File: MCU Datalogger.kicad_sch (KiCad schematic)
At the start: 25 parts, among them U1 24LC1025, U2 24LC1025, U3 DS1337S_, U4 ATMEGA328P-AU, Y1 32.768 KHz, Y2 16 MHz

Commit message: Version for manufacturing
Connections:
- net Vcc: now also BT1.1 (+), C5.1, D2.2 (A), U4.18 (AVCC), U4.4 (VCC)
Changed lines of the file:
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@@
+	)
+	(label "Vcc"
+		(at 254 40.64 0)
+		(effects
+			(font
+				(size 1.27 1.27)
+			)
+			(justify left bottom)
+		)
 	)
 	(label "Vcc"

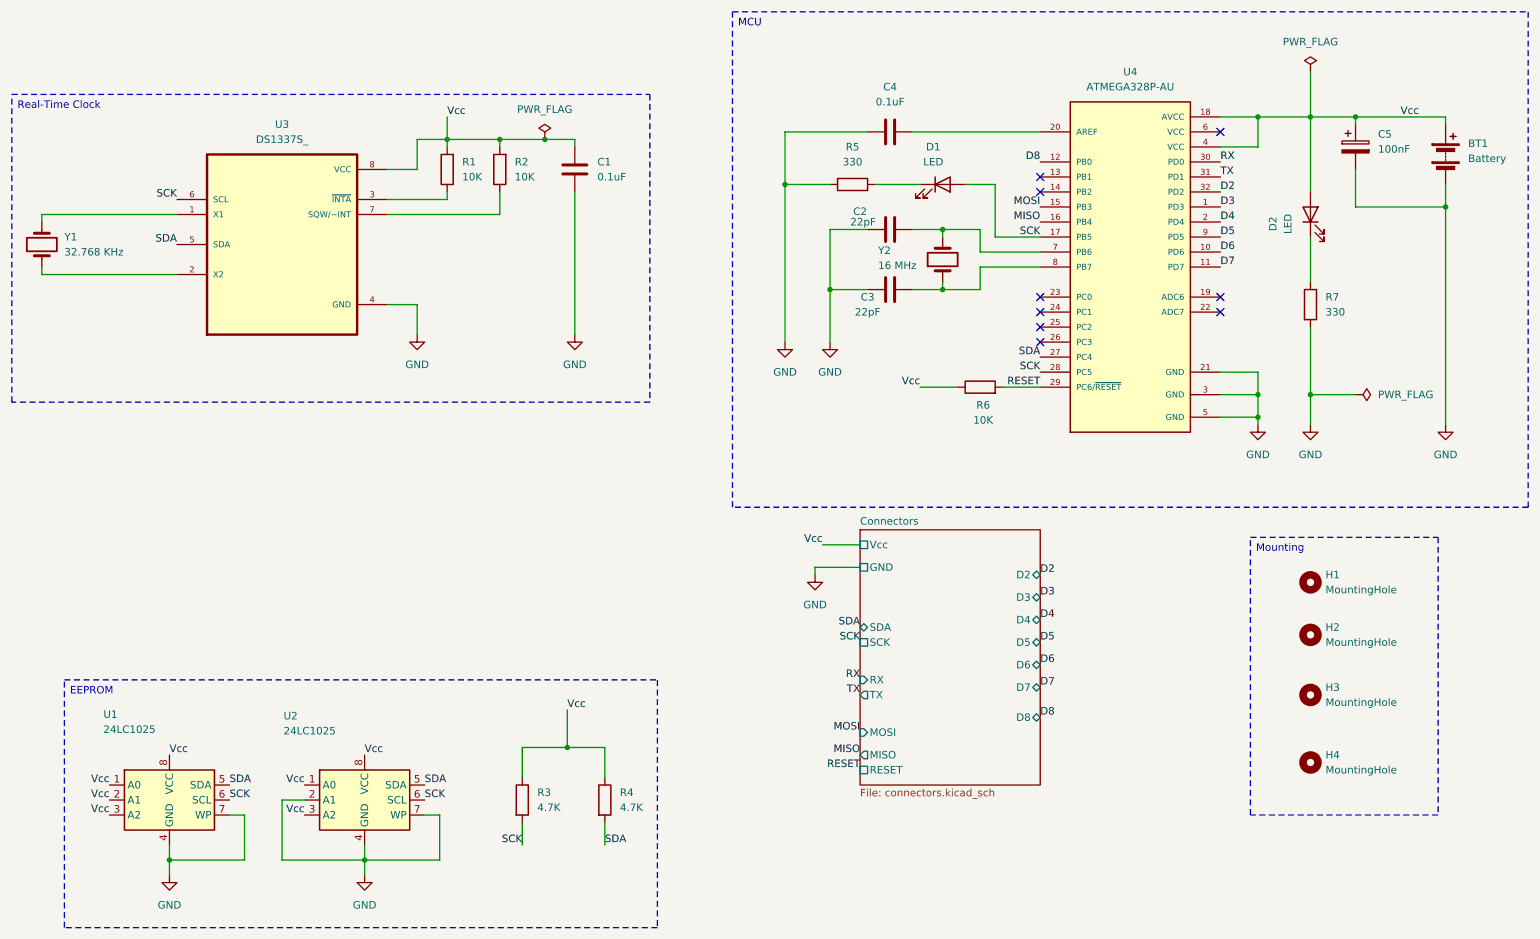
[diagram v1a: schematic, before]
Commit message: Fixed Bugs at 4layer
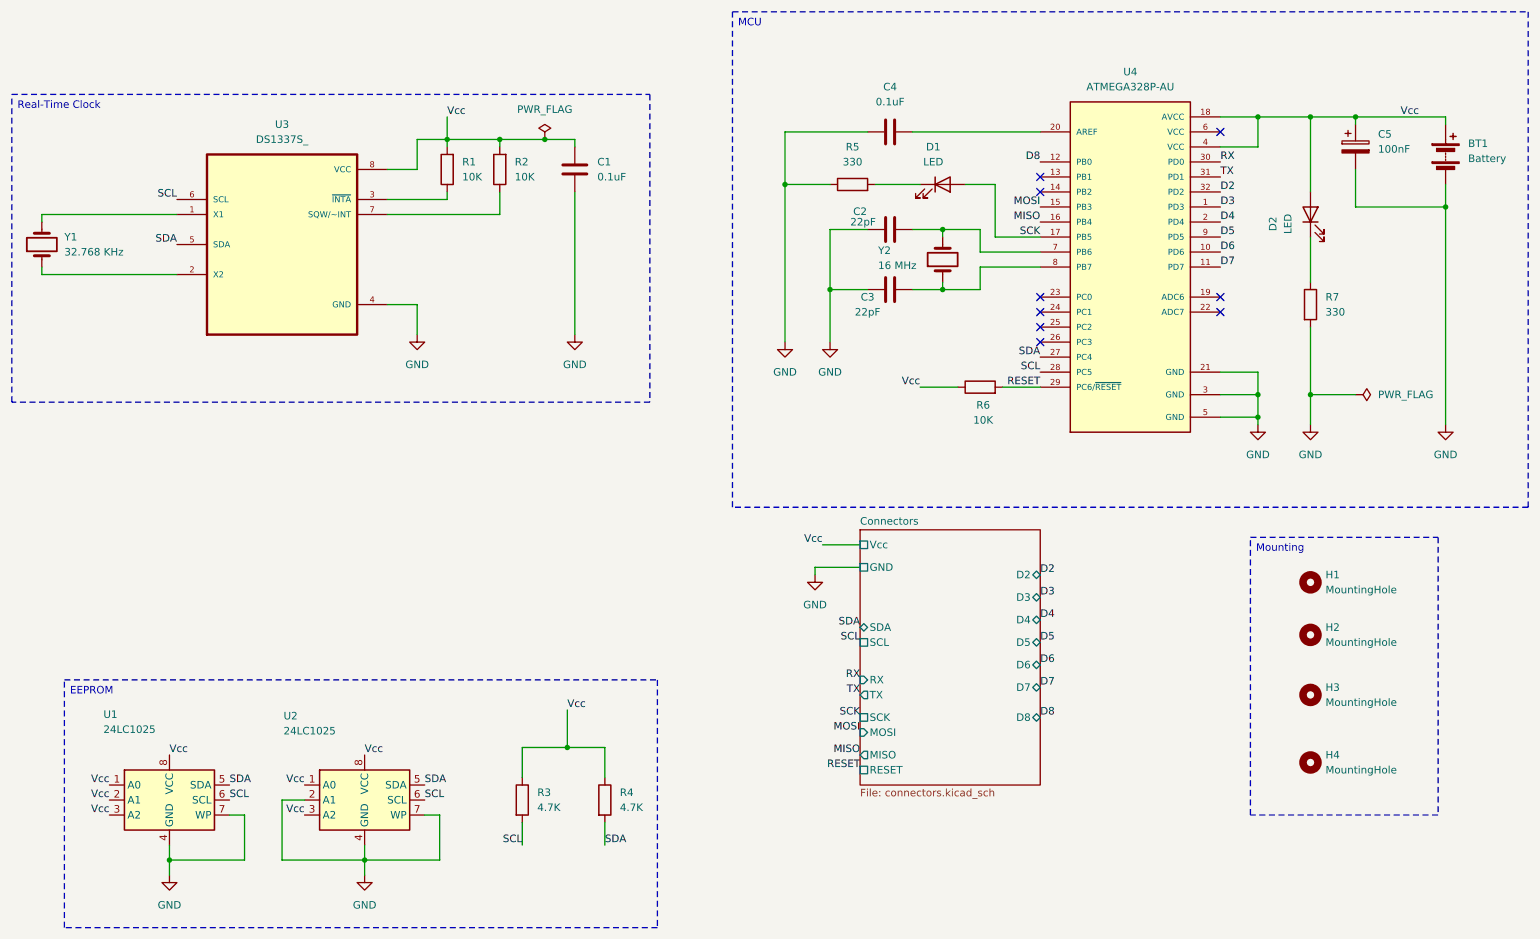
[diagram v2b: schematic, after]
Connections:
- net SCK: no longer R3.2, U1.6 (SCL), U2.6 (SCL), U3.6 (SCL), U4.28 (PC5)
- new net SCL: R3.2, U1.6 (SCL), U2.6 (SCL), U3.6 (SCL), U4.28 (PC5)
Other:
- sheet Connectors ports: added SCL; removed none
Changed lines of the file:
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@@
 	(wire
 		(pts
-			(xy 238.76 33.02) (xy 238.76 40.64)
-		)
-		(stroke
-			(width 0)
-			(type default)
-		)
-	)
-	(wire
-		(pts
 			(xy 82.55 57.15) (xy 101.6 57.15)
 		)
@@
 		)
 	)
+	(label "SCK"
+		(at 162.56 142.24 180)
+		(effects
+			(font
+				(size 1.27 1.27)
+			)
+			(justify right bottom)
+		)
+	)
 	(label "Vcc"
 		(at 35.56 153.67 180)
@@
 		)
 	)
-	(label "SCK"
+	(label "SCL"
 		(at 46.99 54.61 180)
 		(effects
@@
 		)
 	)
-	(label "SCK"
+	(label "SCL"
 		(at 55.88 156.21 0)
 		(effects
@@
 		)
 	)
-	(label "SCK"
+	(label "SCL"
 		(at 88.9 156.21 0)
 		(effects
@@
 		)
 	)
-	(label "SCK"
+	(label "SCL"
 		(at 193.04 83.82 180)
 		(effects
@@
 		)
 	)
-	(label "SCK"
+	(label "SCL"
 		(at 162.56 129.54 180)
 		(effects
@@
 		)
 	)
-	(label "SCK"
+	(label "SCL"
 		(at 105.41 163.83 180)
 		(effects
@@
 	)
 	(symbol
-		(lib_id "power:PWR_FLAG")
-		(at 238.76 33.02 0)
-		(unit 1)
-		(exclude_from_sim no)
-		(in_bom yes)
-		(on_board yes)
-		(dnp no)
-		(fields_autoplaced yes)
-		(property "Reference" "#FLG01"
-			(at 238.76 31.115 0)
-			(effects
-				(font
-					(size 1.27 1.27)
-				)
-				(hide yes)
-			)
-		)
-		(property "Value" "PWR_FLAG"
-			(at 238.76 27.94 0)
-			(effects
-				(font
-					(size 1.27 1.27)
-				)
-			)
-		)
-		(property "Footprint" ""
-			(at 238.76 33.02 0)
-			(effects
-				(font
-					(size 1.27 1.27)
-				)
-				(hide yes)
-			)
-		)
-		(property "Datasheet" "~"
-			(at 238.76 33.02 0)
-			(effects
-				(font
-					(size 1.27 1.27)
-				)
-				(hide yes)
-			)
-		)
-		(property "Description" "Special symbol for telling ERC where power comes from"
-			(at 238.76 33.02 0)
-			(effects
-				(font
-					(size 1.27 1.27)
-				)
-				(hide yes)
-			)
-		)
-		(pin "1"
-		)
-		(instances
-			(project ""
-				(path "/cd3998d6-3bce-4815-b4c8-845bad72b915"
-					(reference "#FLG01")
-					(unit 1)
-				)
-			)
-		)
-	)
-	(symbol
 		(lib_id "Device:R")
 		(at 119.38 156.21 0)
@@
 			)
 		)
-		(pin "SCK" passive
-			(at 162.56 129.54 180)
-			(effects
-				(font
-					(size 1.27 1.27)
-				)
-				(justify left)
-			)
-		)
 		(pin "D8" tri_state
 			(at 193.04 142.24 0)
@@
 			(effects
 				(font
+					(size 1.27 1.27)
+				)
+				(justify left)
+			)
+		)
+		(pin "SCL" passive
+			(at 162.56 129.54 180)
+			(effects
+				(font
+					(size 1.27 1.27)
+				)
+				(justify left)
+			)
+		)
+		(pin "SCK" passive
+			(at 162.56 142.24 180)
+			(effects
+				(font

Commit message: Changed 32.768khz oscillator footprint from 5032 to 3215
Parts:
- Y1: footprint Crystal:Crystal_SMD_5032-2Pin_5.0x3.2mm_HandSoldering -> Crystal:Crystal_SMD_3215-2Pin_3.2x1.5mm
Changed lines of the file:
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@@
 			)
 		)
-		(property "Footprint" "Crystal:Crystal_SMD_5032-2Pin_5.0x3.2mm_HandSoldering"
+		(property "Footprint" "Crystal:Crystal_SMD_3215-2Pin_3.2x1.5mm"
 			(at 24.13 62.23 0)
 			(effects
